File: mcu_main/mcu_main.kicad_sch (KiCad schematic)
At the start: 11 parts, among them U1 ESP32-S3-WROOM-1, U2 USB_C_connector

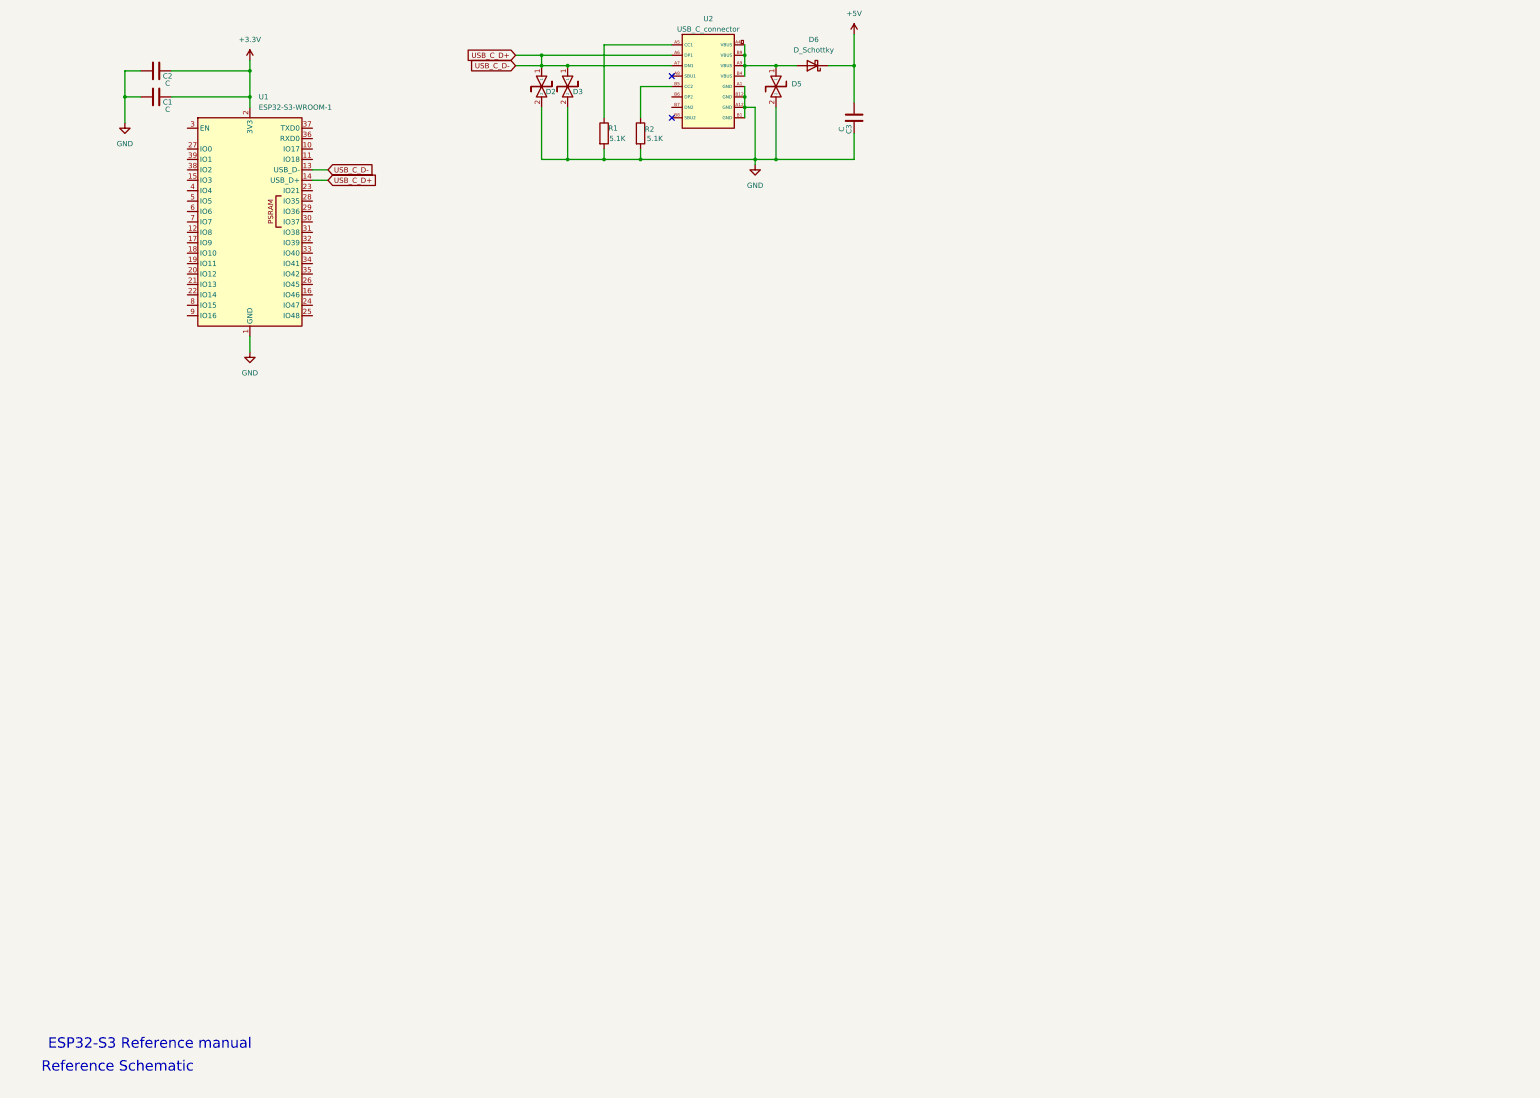
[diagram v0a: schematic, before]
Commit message: setting up hierarchical sheets
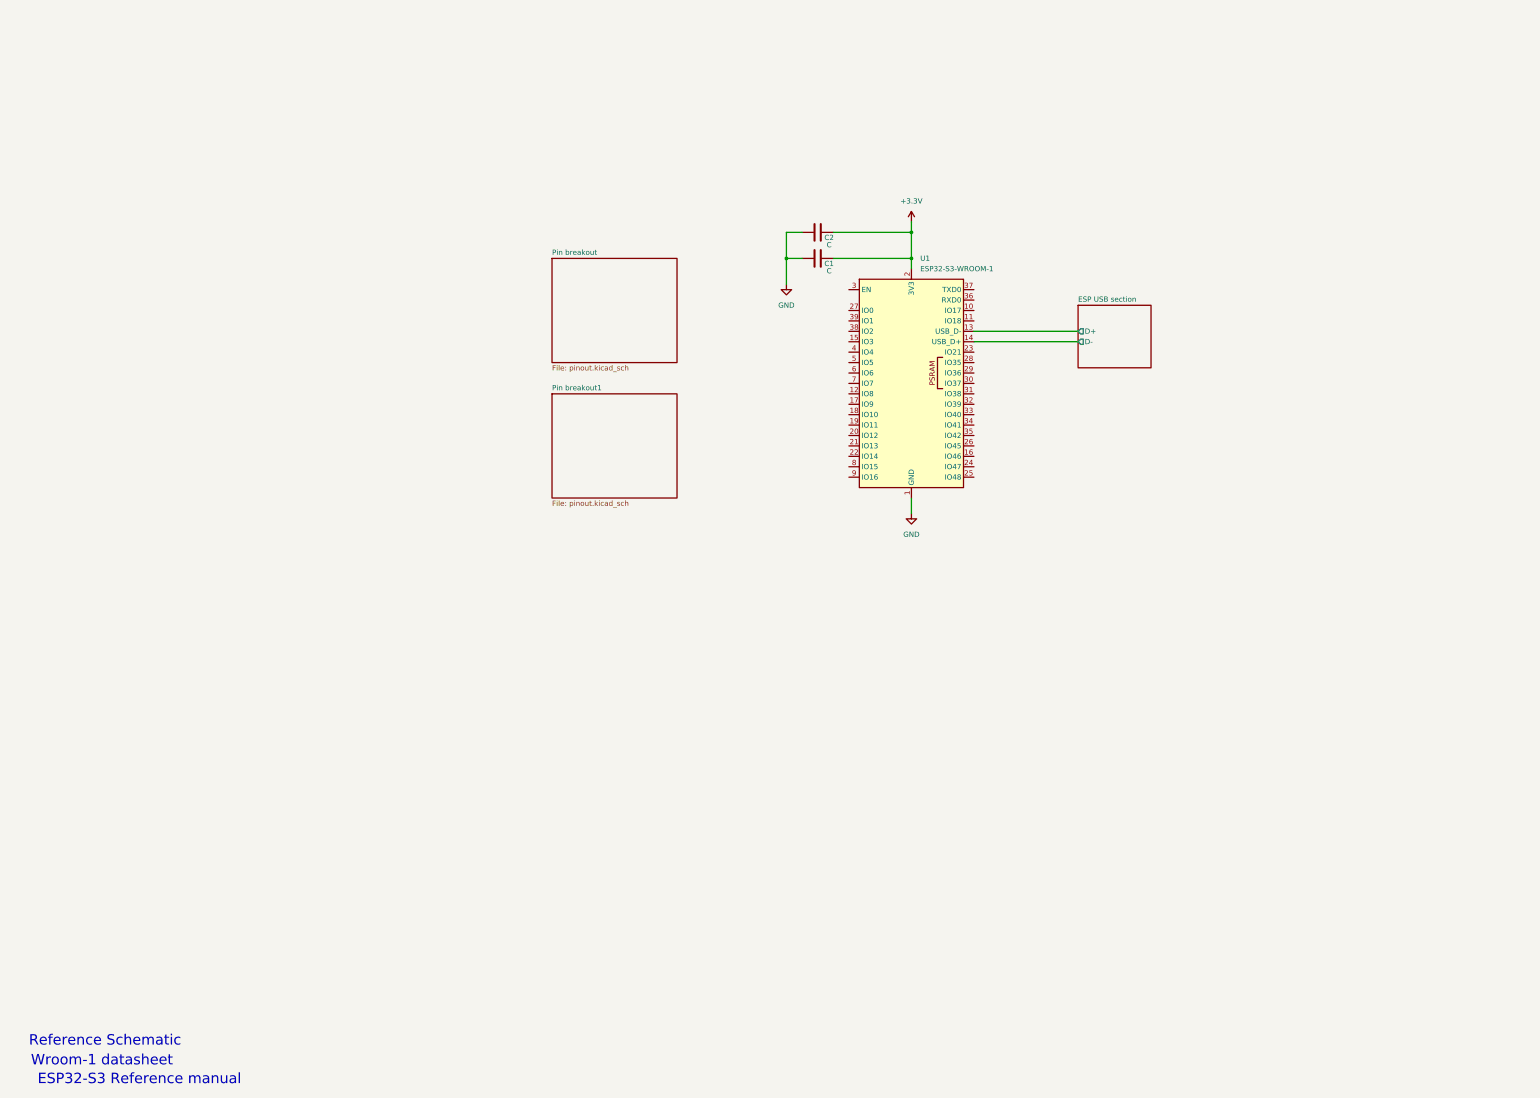
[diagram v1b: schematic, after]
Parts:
- removed C3: C, Capacitor_SMD:C_0603_1608Metric_Pad1.08x0.95mm_HandSolder, symbol Device:C
- removed D2, D3, D5: ~, symbol Custom_symbols:ESD_protection_TVS_RCLAMP0521P-N
- removed D6: D_Schottky, Custom_footprints:SOD_123_schottky_C64885, symbol Device:D_Schottky
- removed R1, R2: 5.1K, symbol Device:R
- removed U2: USB_C_connector, Connector_USB:USB_C_Receptacle_G-Switch_GT-USB-7010ASV, symbol Custom_symbols:USB_C_connector_C165948
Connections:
- net USB_C_D+ renamed ESP USB section/D+
- net ESP USB section/D+: no longer U1.14 (USB_D+)
- new net ESP USB section/D-: U1.14 (USB_D+)
- no-connect marks 2 -> 0
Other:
- added sheet ESP USB section (usb_c_resceptacle.kicad_sch)
- added sheet Pin breakout (pinout.kicad_sch)
- added sheet Pin breakout1 (pinout.kicad_sch)
- note added: "Wroom-1 datasheet"
- moved on the sheet: C1, C2, U1

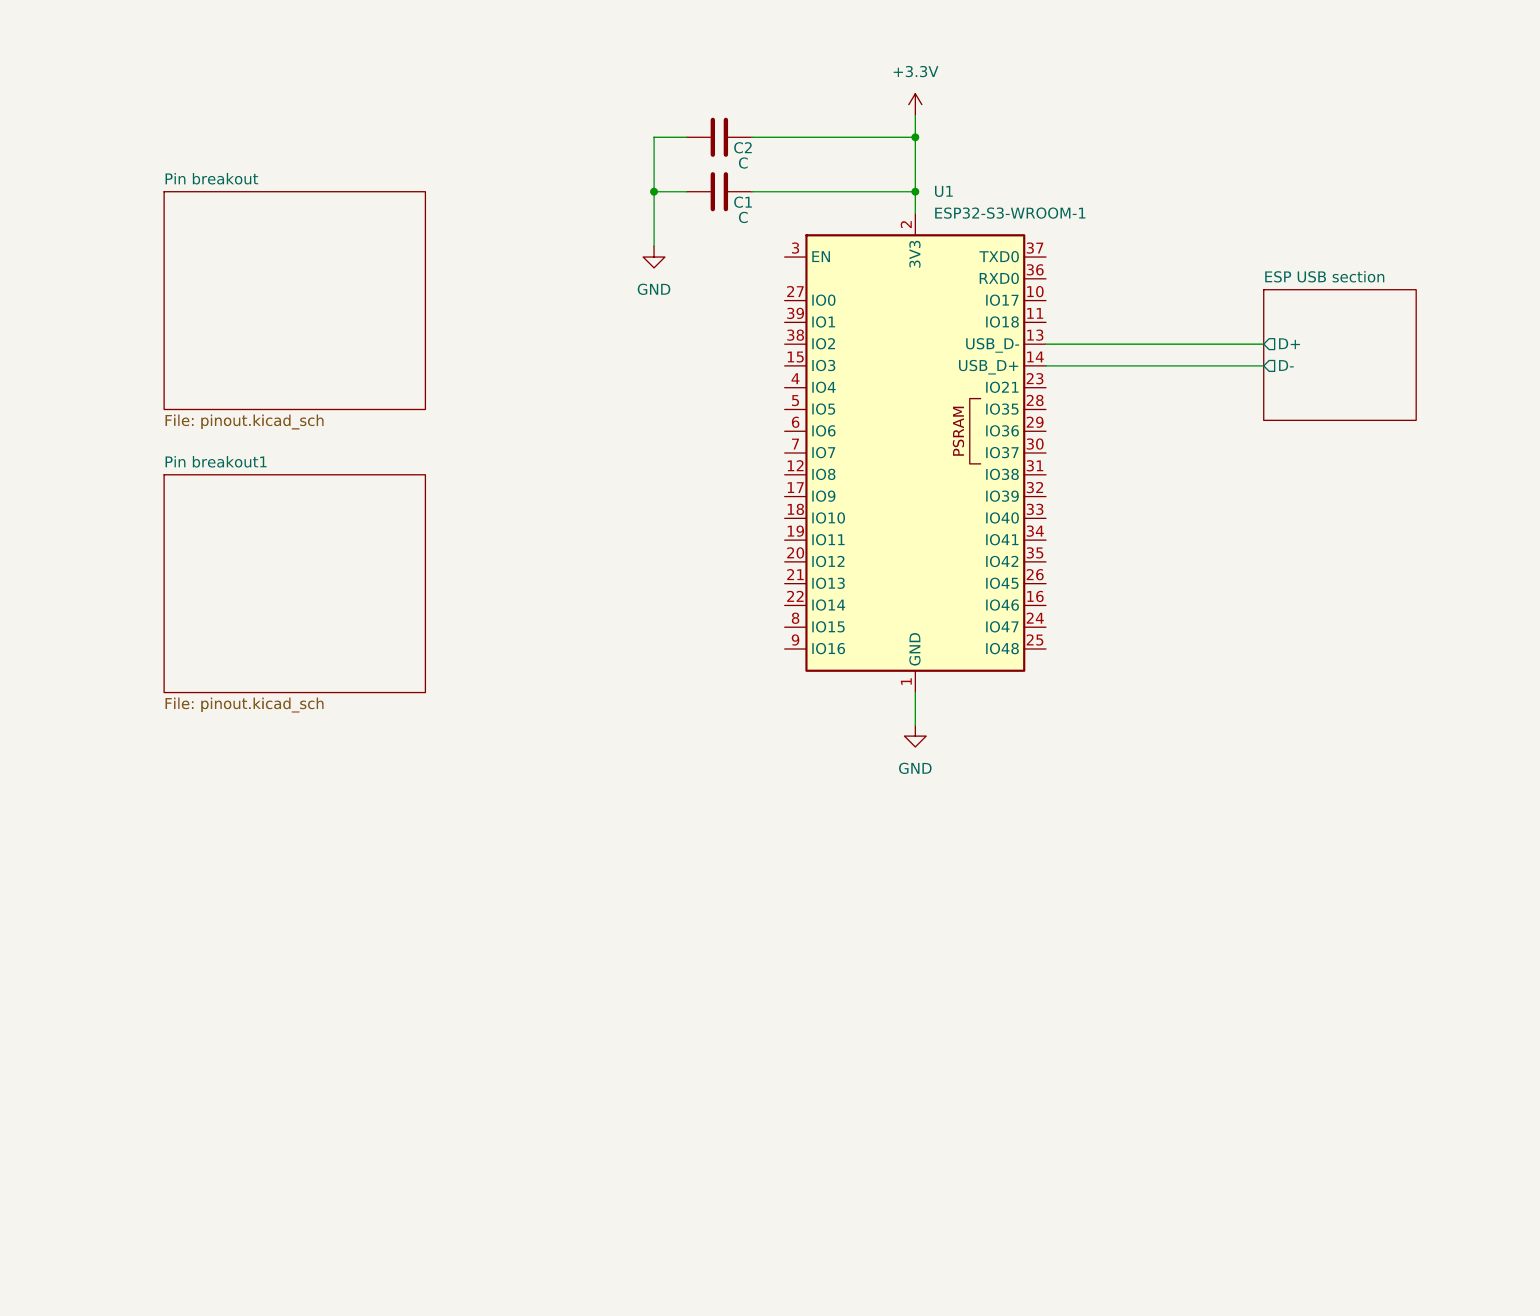
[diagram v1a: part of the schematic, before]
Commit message: adding boot-reset buttons and microsd card spi
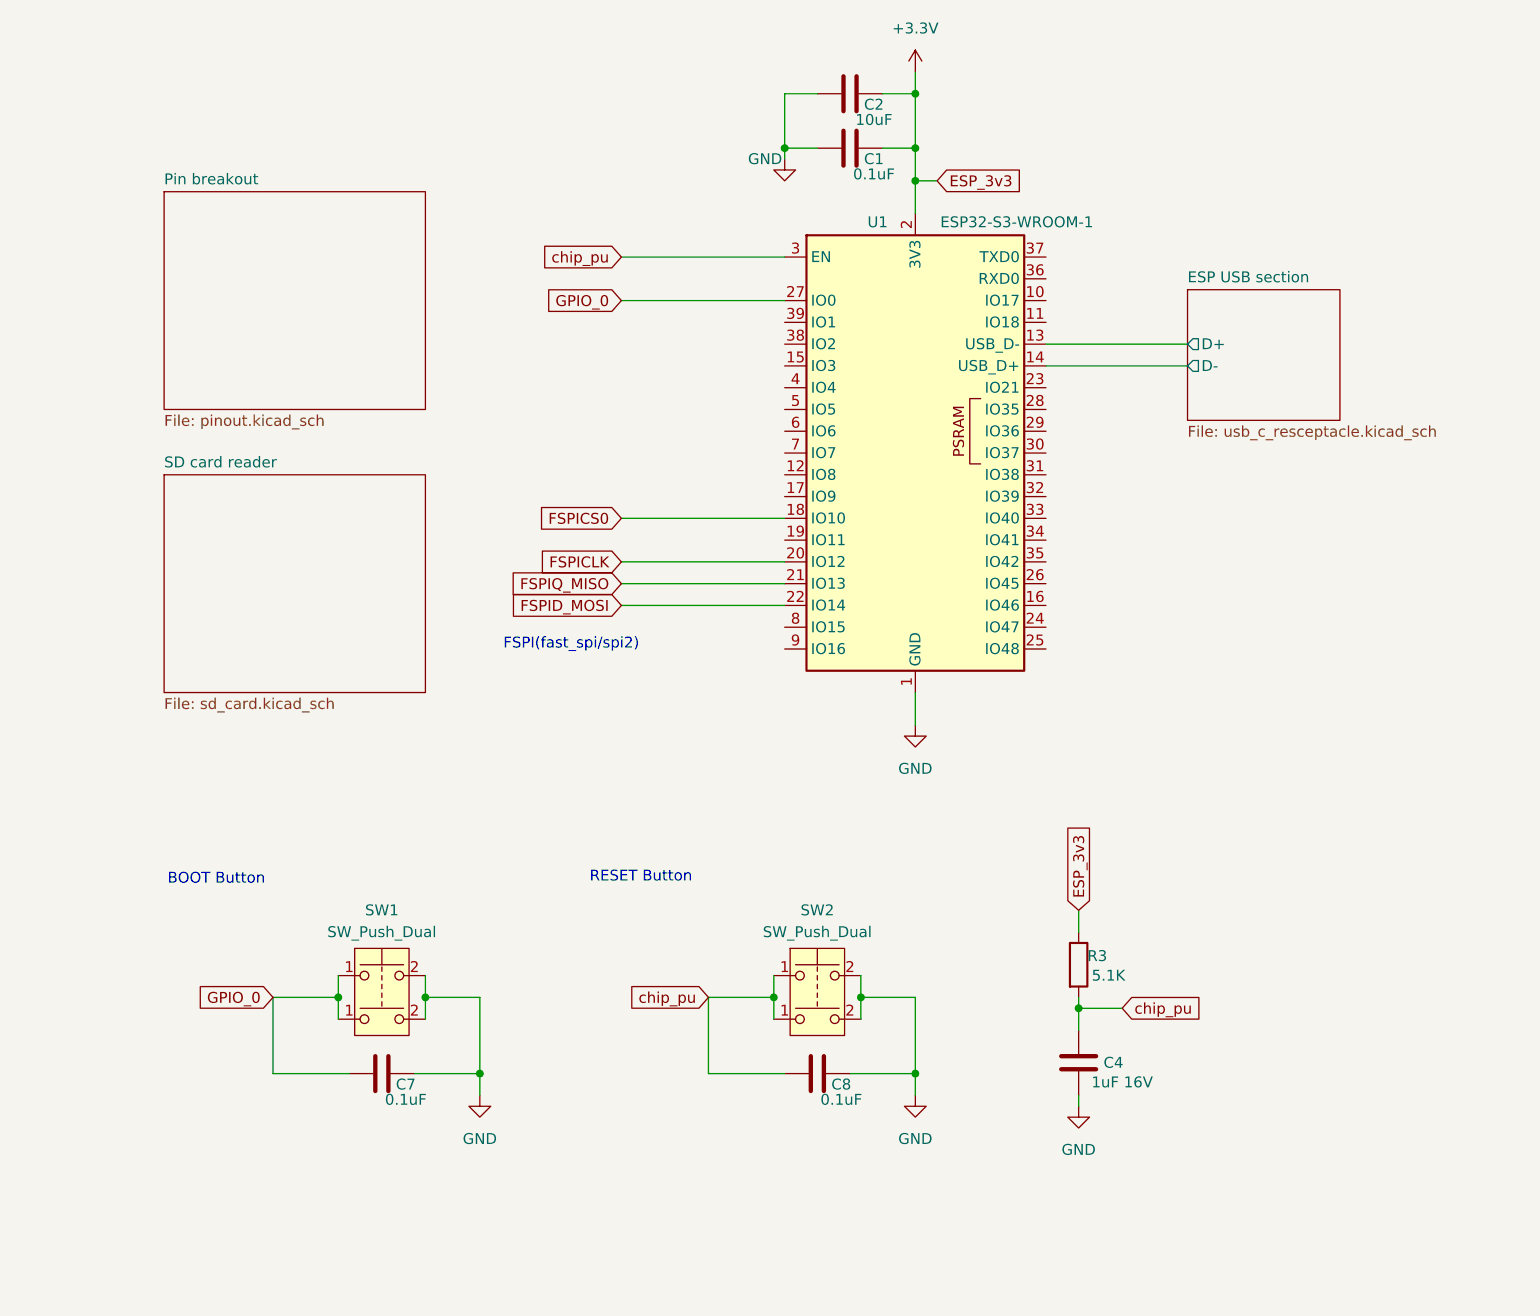
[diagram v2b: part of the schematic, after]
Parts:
- added C4: 1uF 16V, Capacitor_SMD:C_0603_1608Metric_Pad1.08x0.95mm_HandSolder, symbol Device:C
- added C7, C8: 0.1uF, Capacitor_SMD:C_0603_1608Metric_Pad1.08x0.95mm_HandSolder, symbol Device:C
- added R3: 5.1K, Resistor_SMD:R_0805_2012Metric_Pad1.20x1.40mm_HandSolder, symbol Device:R
- added SW1, SW2: SW_Push_Dual, Button_Switch_THT:SW_PUSH_6mm, symbol Switch:SW_Push_Dual
- C1: value C -> 0.1uF
- C2: value C -> 10uF
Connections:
- net +3.3V: now also R3.1
- net GND: now also C4.1, C7.2, C8.2, SW1.2, SW2.2
- net FSPICS0: now reaches U1.18 (IO10)
- net FSPICLK: now reaches U1.20 (IO12)
- net FSPIQ_MISO: now reaches U1.21 (IO13)
- net FSPID_MOSI: now reaches U1.22 (IO14)
- net GPIO_0: now reaches U1.27 (IO0)
- net GPIO_0: now also C7.1, SW1.1
- net chip_pu: now reaches U1.3 (EN)
- net chip_pu: now also C4.2, C8.1, R3.2, SW2.1
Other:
- sheet Pin breakout1 renamed SD card reader
- sheet SD card reader: file pinout.kicad_sch -> sd_card.kicad_sch
- note added: "BOOT Button"
- note added: "FSPI(fast_spi/spi2)"
- note added: "RESET Button"
- moved on the sheet: C1, C2
